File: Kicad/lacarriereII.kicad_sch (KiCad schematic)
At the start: 74 parts, among them J1 USB_C_Receptacle_USB2.0, J2 Conn_02x06, J4 Conn_01x06_Pin, U1 PCA9557PW, U10 XC6206P132MR, U11 ESP32_WROVER, U13 BME280, U15 BME280, U2 BQ25171QWDRCRQ1, U3 CH340C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

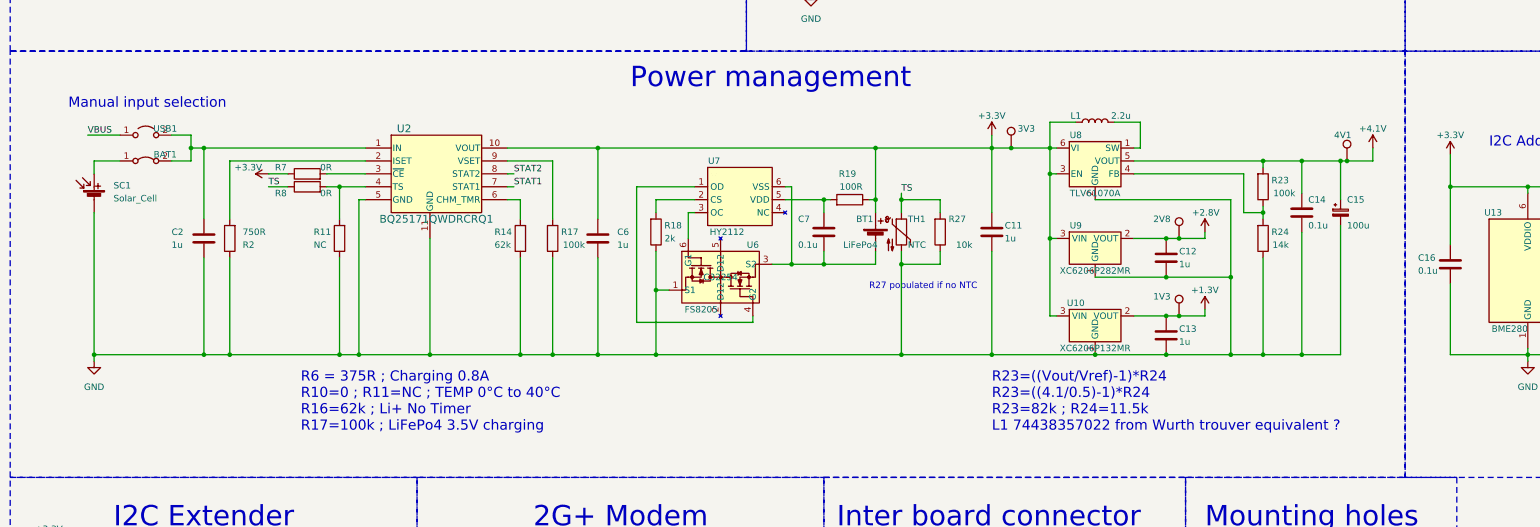
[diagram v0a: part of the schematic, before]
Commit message: [change] ov2640 footprint and add BOM
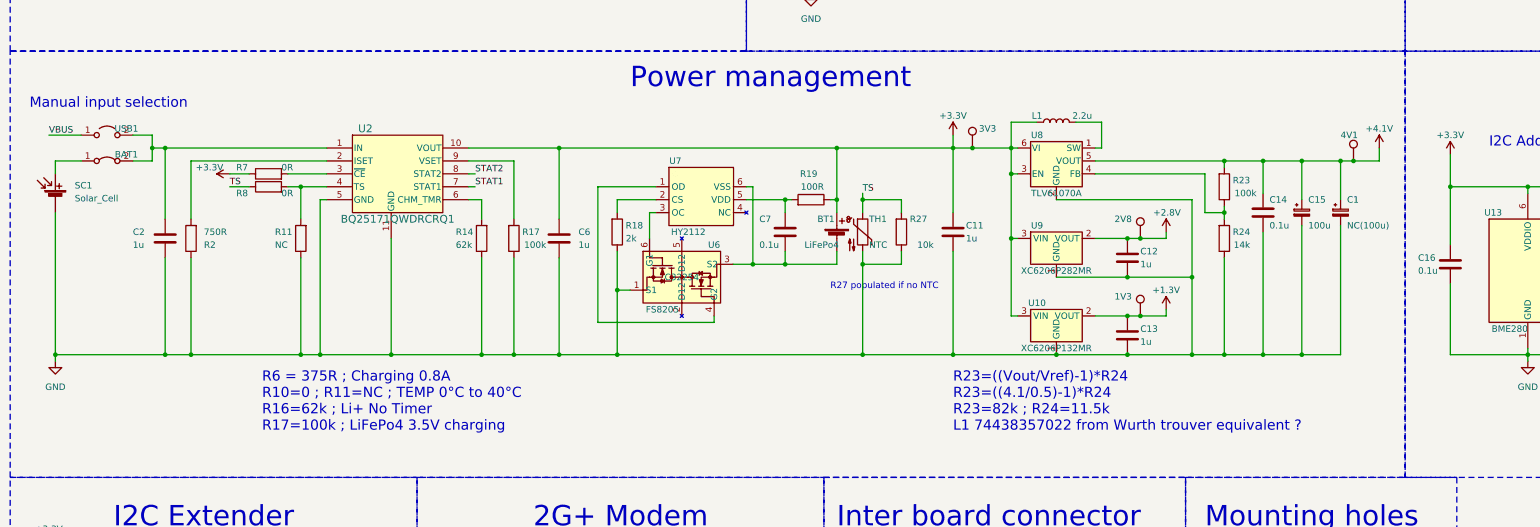
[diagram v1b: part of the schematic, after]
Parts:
- added C1: NC(100u), Capacitor_Tantalum_SMD:CP_EIA-7343-31_Kemet-D_Pad2.25x2.55mm_HandSolder, symbol Device:C_Polarized_Small
- U10, U9: footprint Package_TO_SOT_SMD:SOT-23 -> Package_TO_SOT_SMD:SOT-23-3
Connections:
- net +4V: now also C1.1
- net GND: now also C1.2
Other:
- moved on the sheet: 1V3, 2V8, 3V3, 4V1, BAT1, BT1, C11, C12, C13, C14, C15, C2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
